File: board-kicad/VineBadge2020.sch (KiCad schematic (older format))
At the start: 72 parts

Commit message: tracing vineshroom graphics for board
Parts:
- C1, C2: renamed from C?; footprint (none) -> Capacitors_SMD:C_0603
- D1, D10, D11, D12, D13, D14, D15, D16, D17, D18, D19, D2, D20, D21, D22, D23, D24, D25, D26, D27, D28, D29, D3, D30, D31, D32, D33, D34, D35, D36, D37, D38, D39, D4, D40, D41, D42, D43, D44, D45, D46, D47, D48, D49, D5, D50, D51, D52, D53, D54, D55, D56, D6, D7, D8, D9: renamed from D?; footprint (none) -> LEDs:LED_0603
- F1: renamed from F?; footprint (none) -> Fuse_Holders_and_Fuses:Fuse_SMD1206_Reflow
- IC1: renamed from IC?; footprint TSSOP14 -> SMD_Packages:SSOP-14
- P1: renamed from P?; footprint (none) -> Pin_Headers:Pin_Header_Straight_1x05
- Q1: renamed from Q?; footprint (none) -> TO_SOT_Packages_SMD:SOT-23
- R1, R2, R3, R4, R5, R6, R7, R8: footprint (none) -> Resistors_SMD:R_0805
- R9: renamed from R?; footprint (none) -> Resistors_SMD:R_0805
- gave numbers to parts that had none: 1

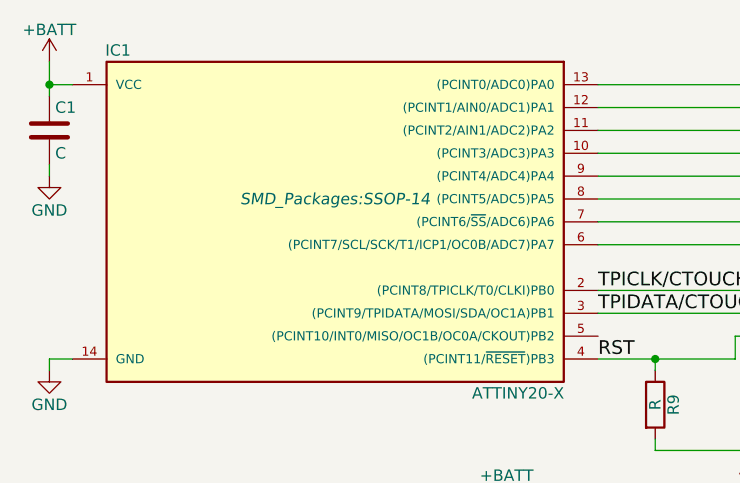
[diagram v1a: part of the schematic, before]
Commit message: starting LED placement
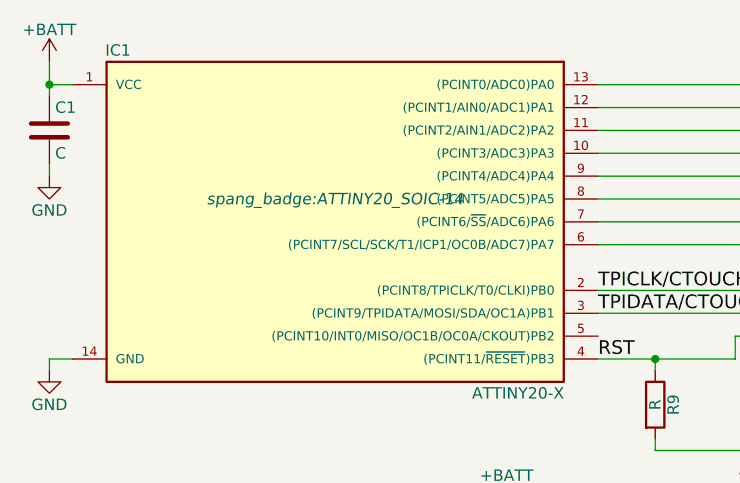
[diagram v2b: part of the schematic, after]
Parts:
- IC1: footprint SMD_Packages:SSOP-14 -> spang_badge:ATTINY20_SOIC-14
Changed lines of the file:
@@
 F 0 "IC1" H 2350 2850 50  0000 C CNN
 F 1 "ATTINY20-X" H 4100 1350 50  0000 C CNN
-F 2 "SMD_Packages:SSOP-14" H 3300 2200 50  0000 C CIN
+F 2 "spang_badge:ATTINY20_SOIC-14" H 3300 2200 50  0000 C CIN
 F 3 "" H 3300 2100 50  0000 C CNN
 	1    3300 2100

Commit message: final touches on shroom badge
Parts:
- removed D53, D54, D55, D56: LED, LEDs:LED_0603, symbol LED
- removed P1: CONN_01X05, Pin_Headers:Pin_Header_Straight_1x05, symbol CONN_01X05
- added J1: CONN-TAGCONNECT-TC2050, vine_badge:TC2050_IDC, symbol CONN-TAGCONNECT-TC2050
- added R10: 1K, Resistors_SMD:R_0805, symbol R
- added SW1: SW_SPST, Buttons_Switches_SMD:SW_SPST_EVQPE1, symbol SW_SPST
- BT1: footprint (none) -> vine_badge:COINCELL_20MM
- R9: value R -> 10K
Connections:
- net +BATT: now also J1.1, R10.2
- net GND: now also J1.3, J1.5, J1.9, SW1.2 (B)
- net RST: now also J1.10
- net BTN: now reaches IC1.5 ((PCINT10/INT0/MISO/OC1B/OC0A/CKOUT)PB2)
- net BTN: now also R10.1, SW1.1 (A)
- net TPICLK/CTOUCH_I renamed TCK
- net TCK: now also J1.4
- net TPIDATA/CTOUCH_O renamed TDI
- net TDI: now also J1.8
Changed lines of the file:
@@
 LIBS:contrib
 LIBS:valves
+LIBS:VineBadge2020
+LIBS:Switch
+LIBS:switches
 LIBS:VineBadge2020-cache
 EELAYER 25 0
@@
 	0    1    1    0
 $EndComp
-$Comp
-L CONN_01X05 P1
-U 1 1 5D1D534A
-P 5500 2600
-F 0 "P1" H 5500 2900 50  0000 C CNN
-F 1 "CONN_01X05" V 5600 2600 50  0000 C CNN
-F 2 "Pin_Headers:Pin_Header_Straight_1x05" H 5500 2600 50  0001 C CNN
-F 3 "" H 5500 2600 50  0000 C CNN
-	1    5500 2600
-	1    0    0    -1
-$EndComp
-$Comp
-L GND #PWR03
-U 1 1 5D1D5CA4
-P 5300 3150
-F 0 "#PWR03" H 5300 2900 50  0001 C CNN
-F 1 "GND" H 5300 3000 50  0000 C CNN
-F 2 "" H 5300 3150 50  0000 C CNN
-F 3 "" H 5300 3150 50  0000 C CNN
-	1    5300 3150
-	1    0    0    -1
-$EndComp
-$Comp
-L +BATT #PWR04
-U 1 1 5D1D5CCC
-P 5100 3150
-F 0 "#PWR04" H 5100 3000 50  0001 C CNN
-F 1 "+BATT" H 5100 3290 50  0000 C CNN
-F 2 "" H 5100 3150 50  0000 C CNN
-F 3 "" H 5100 3150 50  0000 C CNN
-	1    5100 3150
-	-1   0    0    1
-$EndComp
 Text Label 4450 2400 0    60   ~ 0
-TPICLK/CTOUCH_I
+TCK
 Text Label 4450 2500 0    60   ~ 0
-TPIDATA/CTOUCH_O
+TDI
 Text Label 4450 2700 0    60   ~ 0
 RST
@@
 	0    1    1    0
 $EndComp
-$Comp
-L LED D53
-U 1 1 5D1F6ABB
-P 16850 4000
-F 0 "D53" H 16850 4100 50  0000 C CNN
-F 1 "LED" H 16850 3900 50  0000 C CNN
-F 2 "LEDs:LED_0603" H 16850 4000 50  0001 C CNN
-F 3 "" H 16850 4000 50  0000 C CNN
-	1    16850 4000
-	0    -1   -1   0
-$EndComp
-$Comp
-L LED D54
-U 1 1 5D1F6BFD
-P 17150 4000
-F 0 "D54" H 17150 4100 50  0000 C CNN
-F 1 "LED" H 17150 3900 50  0000 C CNN
-F 2 "LEDs:LED_0603" H 17150 4000 50  0001 C CNN
-F 3 "" H 17150 4000 50  0000 C CNN
-	1    17150 4000
-	0    1    1    0
-$EndComp
-$Comp
-L LED D55
-U 1 1 5D1F8217
-P 17450 4050
-F 0 "D55" H 17450 4150 50  0000 C CNN
-F 1 "LED" H 17450 3950 50  0000 C CNN
-F 2 "LEDs:LED_0603" H 17450 4050 50  0001 C CNN
-F 3 "" H 17450 4050 50  0000 C CNN
-	1    17450 4050
-	0    -1   -1   0
-$EndComp
-$Comp
-L LED D56
-U 1 1 5D1F8352
-P 17750 4050
-F 0 "D56" H 17750 4150 50  0000 C CNN
-F 1 "LED" H 17750 3950 50  0000 C CNN
-F 2 "LEDs:LED_0603" H 17750 4050 50  0001 C CNN
-F 3 "" H 17750 4050 50  0000 C CNN
-	1    17750 4050
-	0    1    1    0
-$EndComp
 Wire Wire Line
 	2050 1400 2050 1550
@@
 	5050 2600 5300 2600
 Wire Wire Line
-	5100 2700 5300 2700
-Wire Wire Line
-	5300 2800 5300 3150
-Wire Wire Line
 	4450 2700 5050 2700
 Wire Wire Line
 	5050 2700 5050 2600
-Wire Wire Line
-	5100 2700 5100 3150
 Connection ~ 7250 1500
 Wire Wire Line
@@
 	16550 3850 16550 3800
 Connection ~ 16550 3850
-Wire Wire Line
-	17150 4200 17150 4150
-Connection ~ 17150 4200
-Wire Wire Line
-	17150 1850 17150 3850
-Connection ~ 17150 1850
-Connection ~ 17450 4200
 Wire Wire Line
 	6700 1500 17750 1500
@@
 Connection ~ 12950 3450
 Wire Wire Line
-	7000 3050 12650 3050
-Wire Wire Line
 	13250 2250 13250 3500
 Connection ~ 13250 2250
@@
 	6900 3850 16550 3850
 Wire Wire Line
-	16850 4200 16850 4150
-Connection ~ 16850 4200
-Wire Wire Line
-	16850 3850 16850 1850
-Connection ~ 16850 1850
-Connection ~ 17750 4200
-Wire Wire Line
 	7150 1850 17150 1850
-Wire Wire Line
-	17450 1500 17450 3900
-Connection ~ 17450 1500
-Wire Wire Line
-	17750 1500 17750 3900
-Connection ~ 17750 1500
 Connection ~ 7550 4200
 $Comp
@@
 F 0 "BT1" H 2650 3650 50  0000 L CNN
 F 1 "Battery_Cell" H 2650 3550 50  0000 L CNN
-F 2 "" V 2550 3610 50  0001 C CNN
+F 2 "vine_badge:COINCELL_20MM" V 2550 3610 50  0001 C CNN
 F 3 "" V 2550 3610 50  0000 C CNN
 	1    2550 3550
@@
 	2550 3650 3300 3650
 $Comp
-L GND #PWR05
+L GND #PWR03
 U 1 1 5D236972
 P 4050 3700
-F 0 "#PWR05" H 4050 3450 50  0001 C CNN
+F 0 "#PWR03" H 4050 3450 50  0001 C CNN
 F 1 "GND" H 4050 3550 50  0000 C CNN
 F 2 "" H 4050 3700 50  0000 C CNN
@@
 $EndComp
 $Comp
-L +BATT #PWR06
+L +BATT #PWR04
 U 1 1 5D236A0E
 P 4050 3350
-F 0 "#PWR06" H 4050 3200 50  0001 C CNN
+F 0 "#PWR04" H 4050 3200 50  0001 C CNN
 F 1 "+BATT" H 4050 3490 50  0000 C CNN
 F 2 "" H 4050 3350 50  0000 C CNN
@@
 P 4700 2900
 F 0 "R9" V 4780 2900 50  0000 C CNN
-F 1 "R" V 4700 2900 50  0000 C CNN
+F 1 "10K" V 4700 2900 50  0000 C CNN
 F 2 "Resistors_SMD:R_0805" V 4630 2900 50  0001 C CNN
 F 3 "" H 4700 2900 50  0000 C CNN
@@
 Wire Wire Line
 	4700 3050 4700 3100
-Wire Wire Line
-	4700 3100 5100 3100
-Connection ~ 5100 3100
 $Comp
 L C C1
@@
 Connection ~ 2050 1500
 $Comp
-L GND #PWR07
+L GND #PWR05
 U 1 1 5D239DAF
 P 2050 1900
-F 0 "#PWR07" H 2050 1650 50  0001 C CNN
+F 0 "#PWR05" H 2050 1650 50  0001 C CNN
 F 1 "GND" H 2050 1750 50  0000 C CNN
 F 2 "" H 2050 1900 50  0000 C CNN
@@
 Text Notes 18550 5650 0    60   ~ 12
 0.1
+Wire Wire Line
+	7000 3050 12350 3050
+$Comp
+L CONN-TAGCONNECT-TC2050 J1
+U 1 1 5D6340F6
+P 5550 4000
+F 0 "J1" H 5550 4450 50  0000 C CNN
+F 1 "CONN-TAGCONNECT-TC2050" H 5550 4350 50  0000 C CNN
+F 2 "vine_badge:TC2050_IDC" H 5400 4200 50  0001 C CNN
+F 3 "" H 5400 4200 50  0000 C CNN
+	1    5550 4000
+	1    0    0    -1
+$EndComp
+$Comp
+L +BATT #PWR06
+U 1 1 5D1D5CCC
+P 4700 3100
+F 0 "#PWR06" H 4700 2950 50  0001 C CNN
+F 1 "+BATT" H 4700 3240 50  0000 C CNN
+F 2 "" H 4700 3100 50  0000 C CNN
+F 3 "" H 4700 3100 50  0000 C CNN
+	1    4700 3100
+	-1   0    0    1
+$EndComp
+Connection ~ 5300 2400
+Connection ~ 5300 2500
+Connection ~ 5300 2600
+Wire Wire Line
+	5350 3800 4950 3800
+Wire Wire Line
+	5350 4000 4950 4000
+Wire Wire Line
+	4950 4100 5350 4100
+Wire Wire Line
+	5350 4200 4950 4200
+Wire Wire Line
+	5750 3800 6150 3800
+Wire Wire Line
+	5750 3900 6150 3900
+Wire Wire Line
+	5750 4000 6150 4000
+Connection ~ 6150 3800
+Connection ~ 6150 4000
+Connection ~ 4950 4100
+Text Label 4950 4100 0    60   ~ 0
+TCK
+Text Label 6000 4000 0    60   ~ 0
+TDI
+Text Label 6000 3800 0    60   ~ 0
+RST
+$Comp
+L +BATT #PWR07
+U 1 1 5D638DDE
+P 4950 3800
+F 0 "#PWR07" H 4950 3650 50  0001 C CNN
+F 1 "+BATT" H 4950 3940 50  0000 C CNN
+F 2 "" H 4950 3800 50  0000 C CNN
+F 3 "" H 4950 3800 50  0000 C CNN
+	1    4950 3800
+	0    -1   -1   0
+$EndComp
+$Comp
+L GND #PWR08
+U 1 1 5D638F81
+P 4950 4000
+F 0 "#PWR08" H 4950 3750 50  0001 C CNN
+F 1 "GND" H 4950 3850 50  0000 C CNN
+F 2 "" H 4950 4000 50  0000 C CNN
+F 3 "" H 4950 4000 50  0000 C CNN
+	1    4950 4000
+	0    1    1    0
+$EndComp
+$Comp
+L GND #PWR09
+U 1 1 5D6391AC
+P 4950 4200
+F 0 "#PWR09" H 4950 3950 50  0001 C CNN
+F 1 "GND" H 4950 4050 50  0000 C CNN
+F 2 "" H 4950 4200 50  0000 C CNN
+F 3 "" H 4950 4200 50  0000 C CNN
+	1    4950 4200
+	0    1    1    0
+$EndComp
+$Comp
+L GND #PWR010
+U 1 1 5D6392C7
+P 6150 3900
+F 0 "#PWR010" H 6150 3650 50  0001 C CNN
+F 1 "GND" H 6150 3750 50  0000 C CNN
+F 2 "" H 6150 3900 50  0000 C CNN
+F 3 "" H 6150 3900 50  0000 C CNN
+	1    6150 3900
+	0    -1   -1   0
+$EndComp
+$Comp
+L SW_SPST SW1
+U 1 1 5D63680B
+P 2900 4850
+F 0 "SW1" H 2900 4975 50  0000 C CNN
+F 1 "SW_SPST" H 2900 4750 50  0000 C CNN
+F 2 "Buttons_Switches_SMD:SW_SPST_EVQPE1" H 2900 4850 50  0001 C CNN
+F 3 "" H 2900 4850 50  0001 C CNN
+	1    2900 4850
+	1    0    0    -1
+$EndComp
+Wire Wire Line
+	2400 4850 2700 4850
+Wire Wire Line
+	3100 4850 3400 4850
+Wire Wire Line
+	3400 4850 3400 5050
+$Comp
+L GND #PWR011
+U 1 1 5D63930F
+P 3400 5050
+F 0 "#PWR011" H 3400 4800 50  0001 C CNN
+F 1 "GND" H 3400 4900 50  0000 C CNN
+F 2 "" H 3400 5050 50  0000 C CNN
+F 3 "" H 3400 5050 50  0000 C CNN
+	1    3400 5050
+	1    0    0    -1
+$EndComp
+Wire Wire Line
+	4450 2600 4700 2600
+Connection ~ 4700 2600
+Text Label 4450 2600 0    60   ~ 0
+BTN
+Text Label 2400 4850 0    60   ~ 0
+BTN
+Connection ~ 2400 4850
+$Comp
+L R R10
+U 1 1 5D63DC4D
+P 2700 4650
+F 0 "R10" V 2780 4650 50  0000 C CNN
+F 1 "1K" V 2700 4650 50  0000 C CNN
+F 2 "Resistors_SMD:R_0805" V 2630 4650 50  0001 C CNN
+F 3 "" H 2700 4650 50  0000 C CNN
+	1    2700 4650
+	-1   0    0    1
+$EndComp
+$Comp
+L +BATT #PWR012
+U 1 1 5D63FB11
+P 2700 4450
+F 0 "#PWR012" H 2700 4300 50  0001 C CNN
+F 1 "+BATT" H 2700 4590 50  0000 C CNN
+F 2 "" H 2700 4450 50  0000 C CNN
+F 3 "" H 2700 4450 50  0000 C CNN
+	1    2700 4450
+	1    0    0    -1
+$EndComp
+Wire Wire Line
+	2700 4450 2700 4500
+Wire Wire Line
+	2700 4850 2700 4800
 $EndSCHEMATC

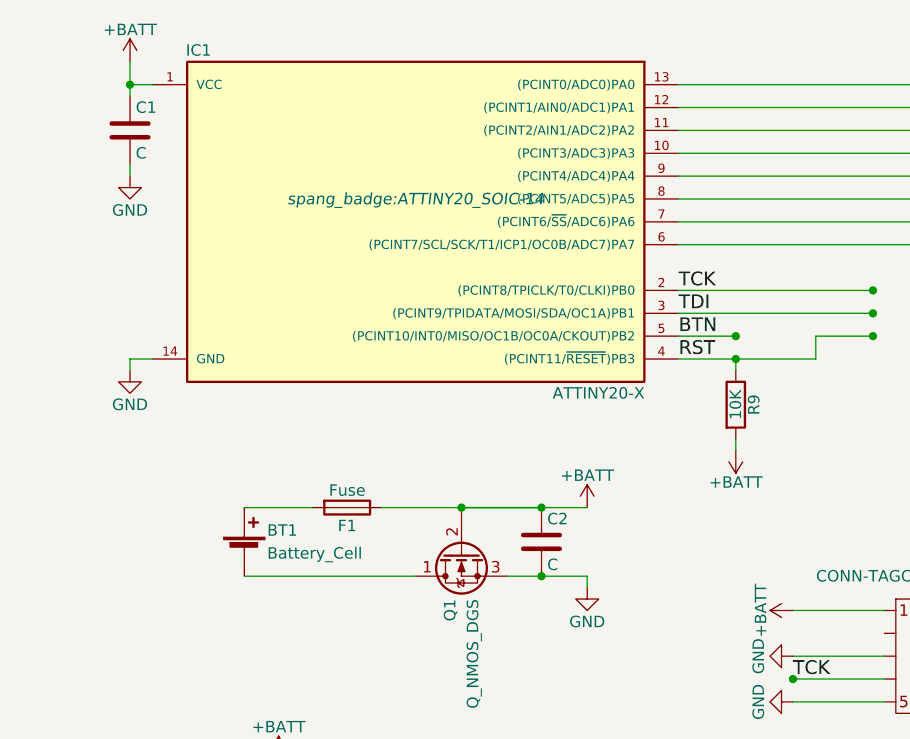
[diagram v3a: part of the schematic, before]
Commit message: working on spang badge v2. TODO: fix B-CU
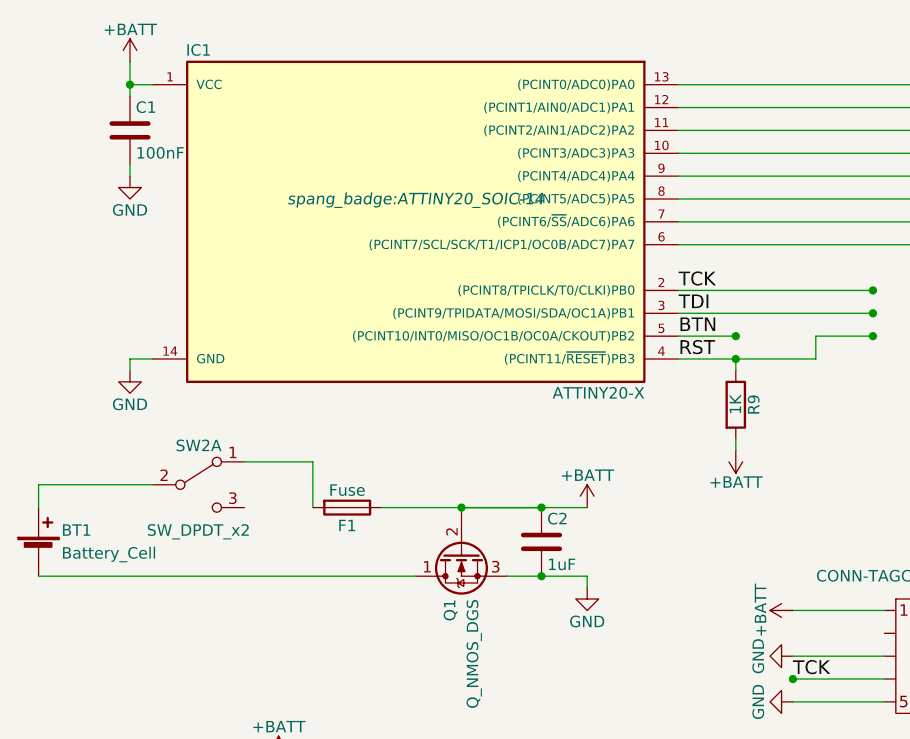
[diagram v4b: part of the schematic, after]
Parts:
- added SW2: SW_DPDT_x2, vine_badge:JS202011JAQN, symbol SW_DPDT_x2
- C1: value C -> 100nF
- C2: value C -> 1uF
- R9: value 10K -> 1K
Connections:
- net at BT1.1 (+): now also SW2.2 (B); no longer F1.2
- new net: F1.2, SW2.1 (A)
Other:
- moved on the sheet: BT1

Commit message: workin on cryptid shroom
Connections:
- net +BATT: now also J1.4; no longer J1.1
- net GND: now also J1.2; no longer J1.3, J1.5, J1.9
- net RST: now also J1.6; no longer J1.10
- net TCK: now also J1.1; no longer J1.4
- net TDI: now also J1.3; no longer J1.8
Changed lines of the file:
@@
 	-1   0    0    1
 $EndComp
-Text Label 4950 4100 0    60   ~ 0
-TCK
-Text Label 6000 4000 0    60   ~ 0
-TDI
-Text Label 6000 3800 0    60   ~ 0
+Text Label 6000 4200 0    60   ~ 0
 RST
-$Comp
-L +BATT #PWR07
-U 1 1 5D638DDE
-P 4950 3800
-F 0 "#PWR07" H 4950 3650 50  0001 C CNN
-F 1 "+BATT" H 4950 3940 50  0000 C CNN
-F 2 "" H 4950 3800 50  0000 C CNN
-F 3 "" H 4950 3800 50  0000 C CNN
-	1    4950 3800
-	0    -1   -1   0
-$EndComp
-$Comp
-L GND #PWR08
-U 1 1 5D638F81
-P 4950 4000
-F 0 "#PWR08" H 4950 3750 50  0001 C CNN
-F 1 "GND" H 4950 3850 50  0000 C CNN
-F 2 "" H 4950 4000 50  0000 C CNN
-F 3 "" H 4950 4000 50  0000 C CNN
-	1    4950 4000
-	0    1    1    0
-$EndComp
-$Comp
-L GND #PWR09
-U 1 1 5D6391AC
-P 4950 4200
-F 0 "#PWR09" H 4950 3950 50  0001 C CNN
-F 1 "GND" H 4950 4050 50  0000 C CNN
-F 2 "" H 4950 4200 50  0000 C CNN
-F 3 "" H 4950 4200 50  0000 C CNN
-	1    4950 4200
-	0    1    1    0
-$EndComp
-$Comp
-L GND #PWR010
-U 1 1 5D6392C7
-P 6150 3900
-F 0 "#PWR010" H 6150 3650 50  0001 C CNN
-F 1 "GND" H 6150 3750 50  0000 C CNN
-F 2 "" H 6150 3900 50  0000 C CNN
-F 3 "" H 6150 3900 50  0000 C CNN
-	1    6150 3900
-	0    -1   -1   0
-$EndComp
 $Comp
 L SW_SPST SW1
@@
 	4950 4100 5350 4100
 Wire Wire Line
-	5350 4200 4950 4200
-Wire Wire Line
-	5750 3800 6150 3800
-Wire Wire Line
-	5750 3900 6150 3900
-Wire Wire Line
-	5750 4000 6150 4000
-Connection ~ 6150 3800
-Connection ~ 6150 4000
-Connection ~ 4950 4100
-Wire Wire Line
 	2400 4850 2700 4850
 Wire Wire Line
@@
 	1    0    0    -1
 $EndComp
+Text Label 4950 3800 0    60   ~ 0
+TCK
+Text Label 4950 4000 0    60   ~ 0
+TDI
+Wire Wire Line
+	6150 4200 5750 4200
+Connection ~ 6150 4200
+Wire Wire Line
+	5350 3900 4950 3900
+Connection ~ 4950 4000
+Connection ~ 4950 3800
+$Comp
+L +BATT #PWR?
+U 1 1 5D874440
+P 4950 4100
+F 0 "#PWR?" H 4950 3950 50  0001 C CNN
+F 1 "+BATT" H 4950 4240 50  0000 C CNN
+F 2 "" H 4950 4100 50  0000 C CNN
+F 3 "" H 4950 4100 50  0000 C CNN
+	1    4950 4100
+	0    -1   -1   0
+$EndComp
+$Comp
+L GND #PWR?
+U 1 1 5D8784AD
+P 4950 3900
+F 0 "#PWR?" H 4950 3650 50  0001 C CNN
+F 1 "GND" H 4950 3750 50  0000 C CNN
+F 2 "" H 4950 3900 50  0000 C CNN
+F 3 "" H 4950 3900 50  0000 C CNN
+	1    4950 3900
+	0    1    1    0
+$EndComp
 $EndSCHEMATC
